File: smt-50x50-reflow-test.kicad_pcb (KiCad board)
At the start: 4 copper layers, 50 x 50 mm, 96 parts, among them J1 Conn_01x04_Pin, J2 Conn_01x02, J4 USB_C_Receptacle_USB2.0_14P, J8 Conn_01x04_Pin, J9 Conn_01x03_Pin, SW1 SW_Push, SW2 SW_Push, U1 ESP32-C6, U14 TMP117AIDRV, U15 BMP581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

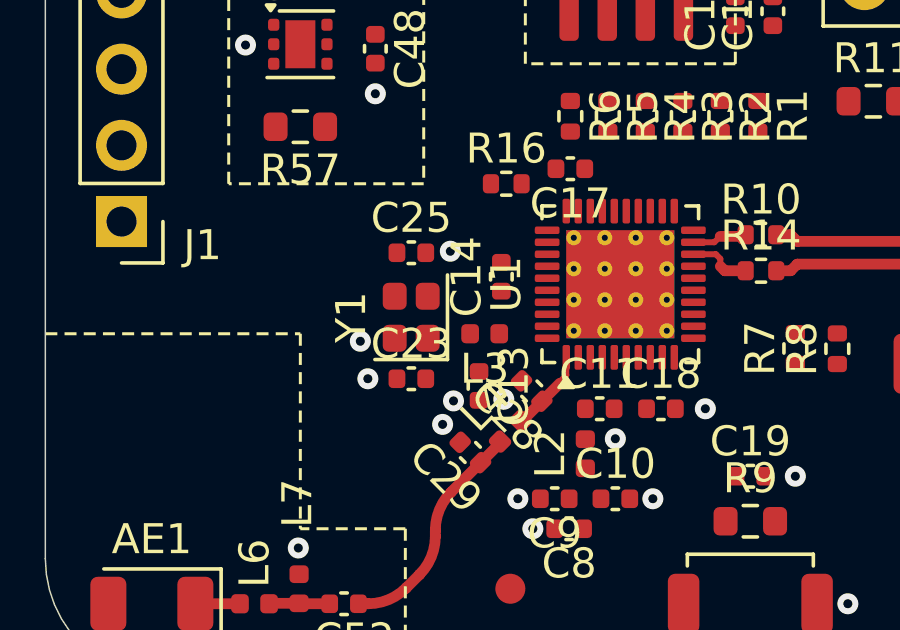
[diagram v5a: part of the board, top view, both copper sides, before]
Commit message: pcb: add crystal routing
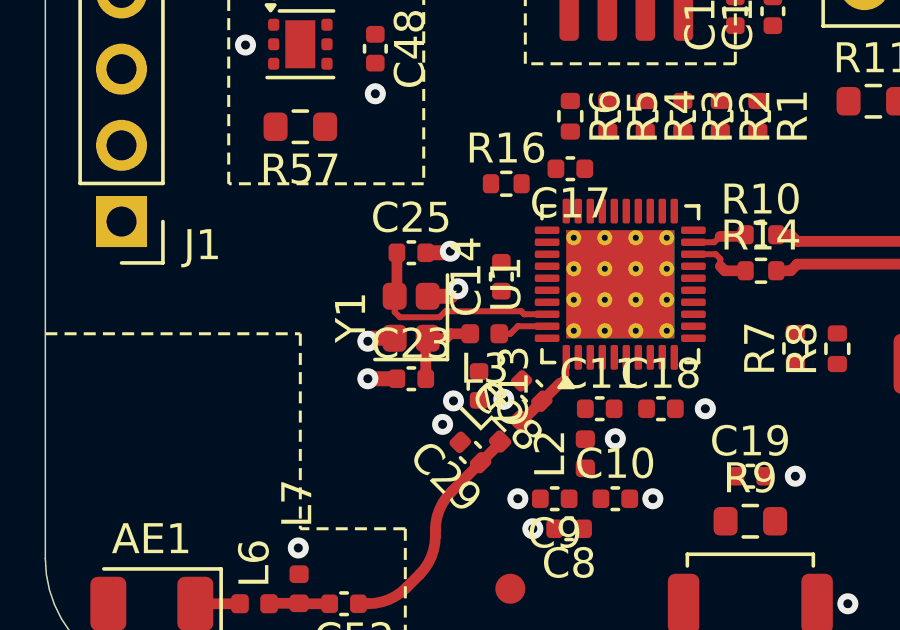
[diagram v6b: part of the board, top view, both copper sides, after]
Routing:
- net /XTAL_N: track 0.00 -> 7.29 mm
- net GND: track 0.00 -> 3.86 mm, vias 42 -> 43
- net /XTAL_PL: track 0.00 -> 2.85 mm
- net /XTAL_P: track 0.00 -> 1.70 mm

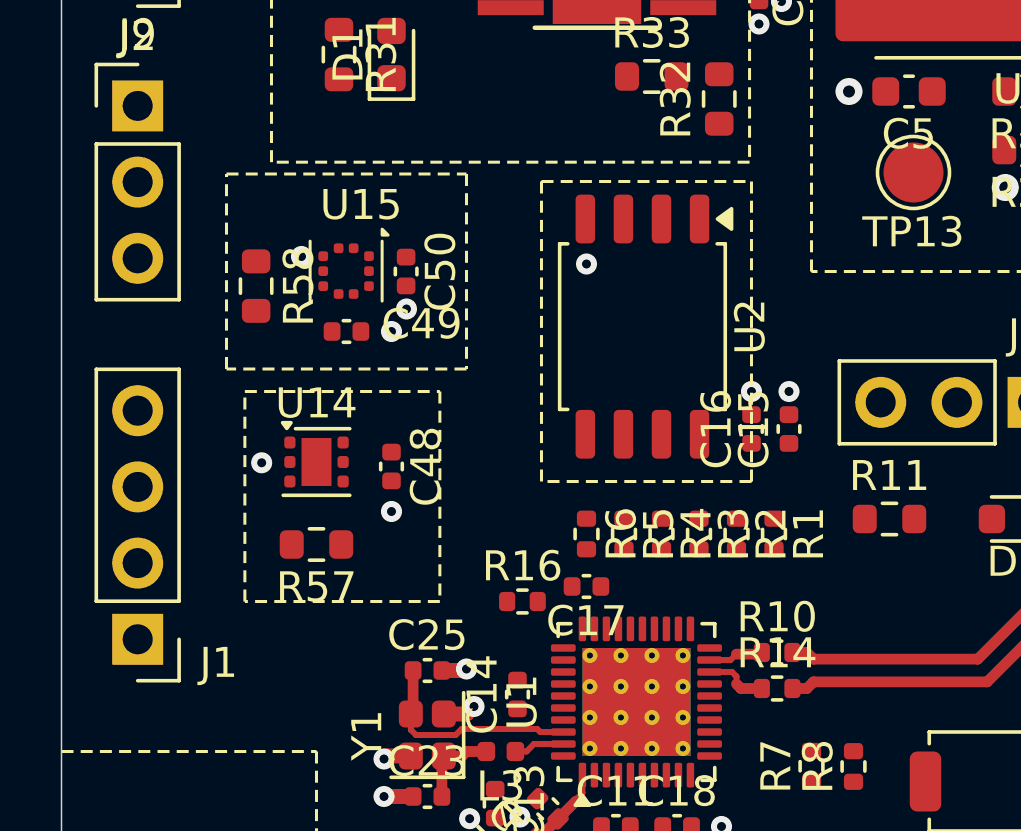
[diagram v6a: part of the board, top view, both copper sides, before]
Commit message: pcb: add SPI FLASH routing
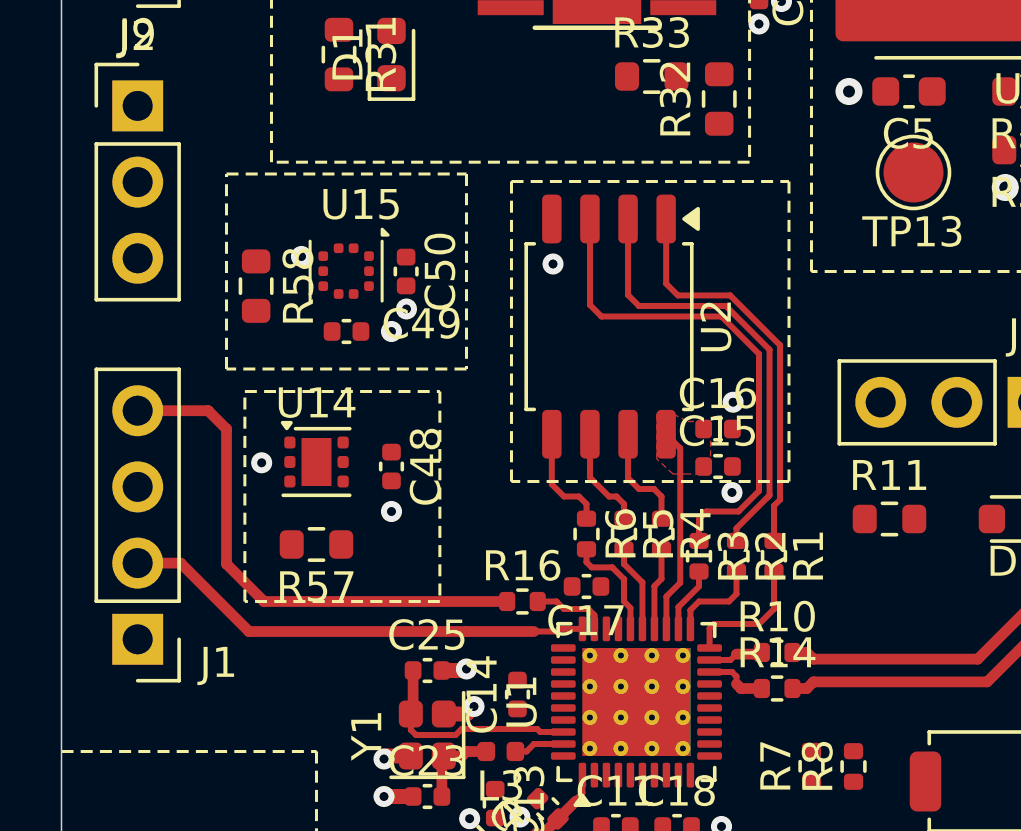
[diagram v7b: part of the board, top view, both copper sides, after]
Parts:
- moved C15 2.68 mm to (156.9, 104.0), turned to 0 degrees
- moved C16 1.12 mm to (156.9, 102.8), turned to 0 degrees
- moved U2 1.12 mm to (153.2, 99.3)
- moved R1 0.74 mm to (158.8, 107.0)
- moved R2 0.74 mm to (157.5, 107.0)
- moved R3 0.74 mm to (156.2, 107.0)
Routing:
- net Net-(J1-Pin_4): track 0.00 -> 17.6 mm
- net Net-(U2-~{WP}/IO_{2}): track 0.00 -> 16.9 mm
- net /U0RXD: track 0.00 -> 15.8 mm
- net Net-(U2-DO/IO_{1}): track 0.00 -> 14.8 mm
- net Net-(U2-~{CS}): track 0.00 -> 13.4 mm
- net Net-(U1-VDD_SPI/GPIO27): track 0.00 -> 6.87 mm
- net Net-(U1-SPICS0/GPIO24): track 0.00 -> 4.32 mm
- net Net-(U1-SPID/GPIO30): track 0.00 -> 3.66 mm
- net Net-(U2-DI/IO_{0}): track 0.00 -> 3.64 mm
- net Net-(U2-~{HOLD}/~{RESET}/IO_{3}): track 0.00 -> 3.57 mm
- net Net-(U2-CLK): track 0.00 -> 3.46 mm
- net Net-(U1-SPIQ/GPIO25): track 0.00 -> 3.13 mm
- net Net-(U1-SPICLK/GPIO29): track 0.00 -> 2.91 mm
- net Net-(U1-SPIHD/GPIO28): track 0.00 -> 2.75 mm
- net /U0TXD: track 0.00 -> 2.54 mm
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- added copper zone on F.Cu, net Net-(U1-VDD_SPI/GPIO27)

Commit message: pcb: add SMPS routing
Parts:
- moved TP15 0.25 mm to (143.8, 79.8)
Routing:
- net +5V: track 0.00 -> 24.0 mm, vias 0 -> 2
- net Net-(D1-A): track 0.00 -> 6.06 mm
- net Net-(U5-BOOT): track 0.00 -> 2.60 mm
- net Net-(U5-VCC): track 0.00 -> 2.56 mm
- added copper zone on F.Cu, net GND
- added copper zone on F.Cu, net Net-(J2-Pin_1)
- added copper zone on F.Cu, net Net-(U5-FB)
- added copper zone on F.Cu, net Net-(U5-SW)
